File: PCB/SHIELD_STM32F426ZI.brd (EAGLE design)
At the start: 83 x 120.2 mm, 15 parts, among them Q1 FDN304P

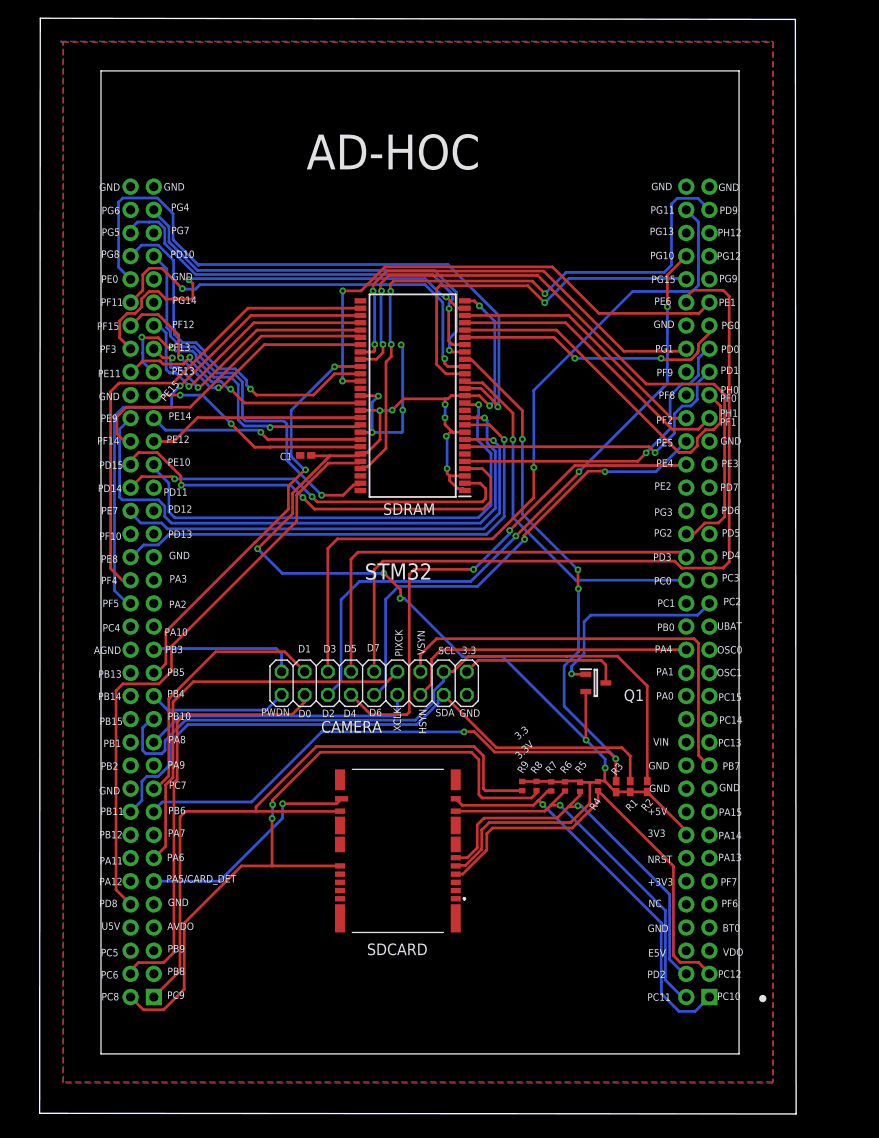
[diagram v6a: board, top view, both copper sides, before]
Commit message: new position camrera and pir sensor
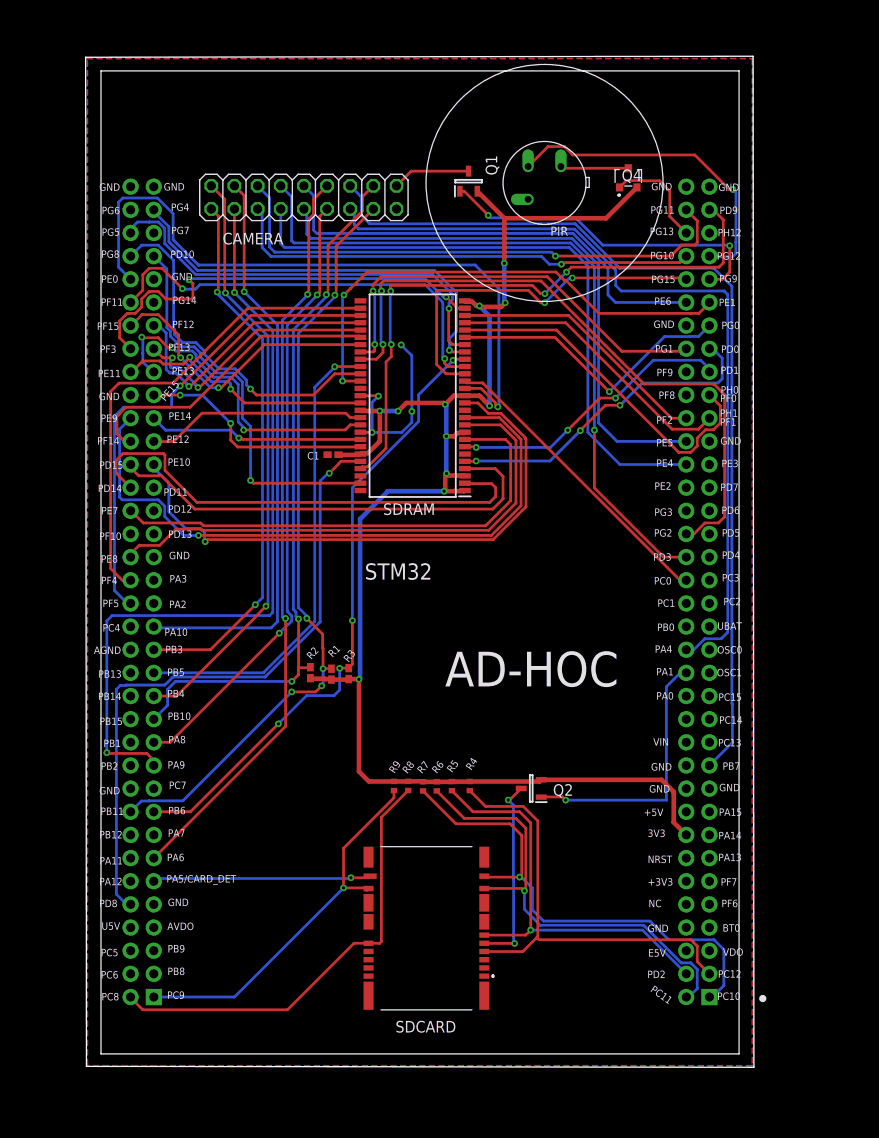
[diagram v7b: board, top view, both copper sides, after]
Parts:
- added PIR: SENBA_PIR_3PIN, sicom_universal:SENBA_PIR
- added Q2: FDN304P, FDN304P:SOT95P237X112-3N
- added Q4: SSM3J338R,LF, SamacSys_Parts:SSM3J332RLFT
- moved Q1 56.8 mm to (50.2, 102.7), turned to 90 degrees
- moved CAMERA 53.9 mm to (32.1, 100.9)
- moved R2 39.0 mm to (32.9, 48.8)
- moved R1 35.0 mm to (35.2, 48.6)
- moved R3 31.9 mm to (37.0, 48.7)
- moved R6 14.1 mm to (46.7, 36.3)
- moved R7 14.1 mm to (45.2, 36.3)
- moved R9 14.1 mm to (42.0, 36.4)
- moved R4 14.1 mm to (50.3, 36.3)
- moved R8 14.1 mm to (43.6, 36.4)
- moved R5 14.1 mm to (48.4, 36.3)
- moved SDCARD 9.05 mm to (45.6, 11.8)
- moved C1 3.00 mm to (35.3, 72.7)
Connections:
- new net MOSFET_SDCARD: Q2.1, STM32.CN11_30
- new net N$1: Q2.3, SDCARD.10
- new net PIR_3V3: PIR.P$2, Q4.3
- new net PIR_EN: Q4.1, STM32.CN11_68
- new net PIR_INT: PIR.P$1, STM32.CN11_65
- net 3.3V: now also Q2.2, Q4.2; no longer SDCARD.10
- net DCMI_D0: now also STM32.CN12_21; no longer STM32.CN12_4
- net DCMI_D1: now also STM32.CN12_33; no longer STM32.CN12_19
- net GATE: now also STM32.CN11_63; no longer STM32.CN11_35
- net GND: now also PIR.P$3
- net PWDN: now also STM32.CN12_31; no longer STM32.CN12_27
- net RESET: now also STM32.CN12_27; no longer STM32.CN12_31
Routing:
- net DCMI_HSYNC: track 32.8 -> 89.4 mm
- net DCMI_VSYNC: track 47.3 -> 101.3 mm
- net RESET: track 16.3 -> 65.2 mm, vias 0 -> 2
- net PWDN: track 15.4 -> 59.4 mm, vias 0 -> 2
- net FMC_SDNE1: track 110.5 -> 69.2 mm, vias 5 -> 4
- net DCMI_PIXCK: track 44.0 -> 82.4 mm, vias 0 -> 2
- net DCMI_D0: track 47.1 -> 85.1 mm, vias 0 -> 2
- net RCC_MCO_1: track 30.1 -> 67.9 mm, vias 0 -> 2
- net PIR_INT: track 0.00 -> 35.6 mm, vias 0 -> 1
- net DCMI_D1: track 28.6 -> 63.7 mm, vias 0 -> 1
- net DCMI_D7: track 86.1 -> 51.2 mm
- net SDIO_D1: track 75.3 -> 41.7 mm, vias 0 -> 1
- net MOSFET_SDCARD: track 0.00 -> 29.1 mm, vias 0 -> 1
- net DCMI_D5: track 49.7 -> 78.4 mm, vias 0 -> 1
- net SDIO_D0: track 77.5 -> 49.0 mm, vias 2 -> 0
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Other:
- board size 83 x 120.2 mm -> 73.3 x 110.9 mm
- board text removed: "3.3"
- board text removed: "3.3V"
- board text removed: "D0"
- board text removed: "D1"
- board text removed: "D2"
- board text removed: "D3"
- board text removed: "D4"
- board text removed: "D5"
- board text removed: "D6"
- board text removed: "D7"
- board text removed: "HSYN"
- board text removed: "PIXCK"
- board text removed: "PWDN"
- board text removed: "SCL"
- board text removed: "SDA"
- board text removed: "VSYN"
- board text removed: "XCLK"

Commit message: new position camera and add pir sensor
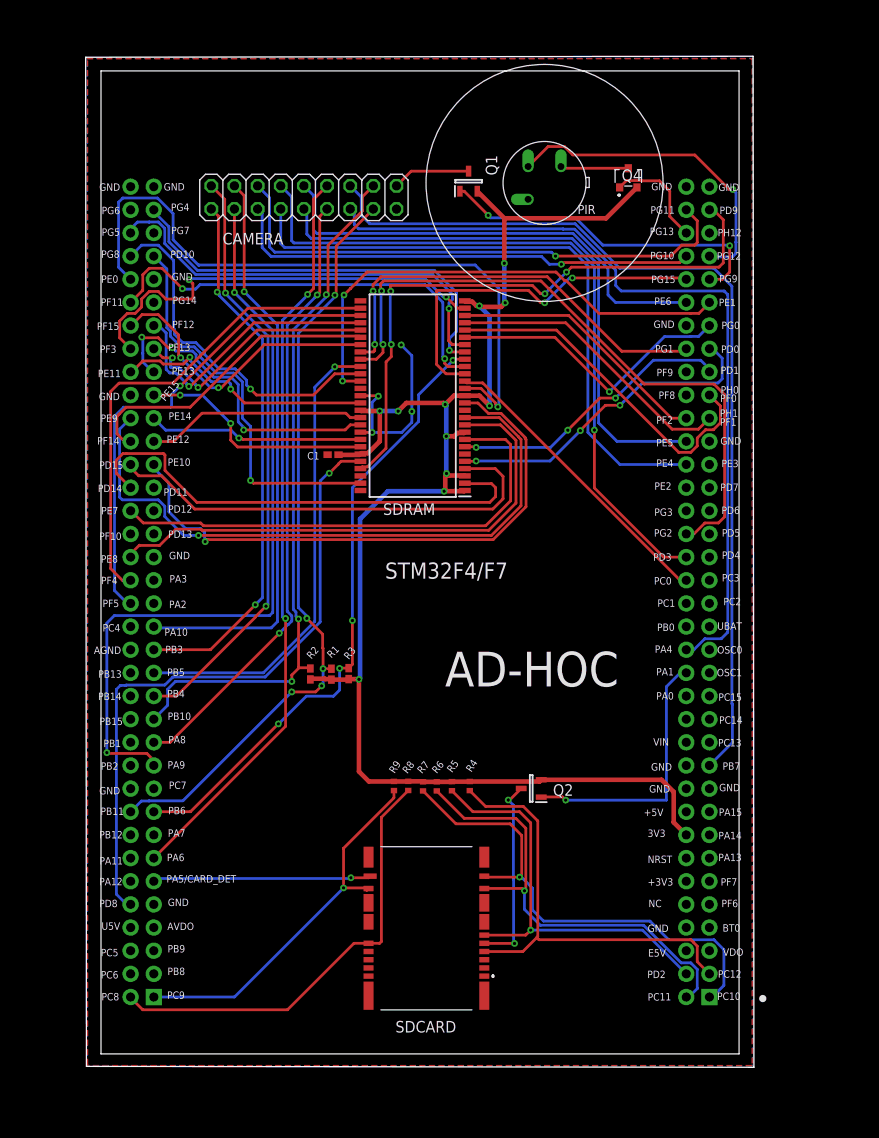
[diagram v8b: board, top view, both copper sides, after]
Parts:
- moved R2 0.14 mm to (32.9, 48.6)
- renumbered STM32 to STM32F4/F7
